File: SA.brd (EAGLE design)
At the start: 60 x 75 mm, 171 parts, among them CON1 RF_IN, CON2 PLL_OUT, CON3 SWD_CON, CON4 USB-C, IC1 RF_AMP, IC10 MCP6D11, IC11 MCP6D11, IC12 TAR5SB33, IC2 STW81200, IC3 ADL5380, IC4 TAR5SB33, IC5 STM32G431KB, IC6 SKY13453, IC7 NJG1809, IC8 SKY13453, IC9 NJG1809, J1 HW_PD, T1 X4B40L1, X1 25MHz, X2 25MHz, X3 12MHz

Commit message: ほぼ完成
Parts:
- removed R2: 10, my_rcl:1608
- added C82: 0.1u, my_rcl:1608C
- added C83: 100p, my_rcl:1608C
- added L10: 47nH, my_rcl:1005
- added R40: 10k, my_rcl:1608
- added SW1: BOOT0, my_rcl:SKRPACE010
- C25, C27, C55: value 22p -> 100p; device my_rcl:1608C -> my_rcl:1005
- C26, C28, C3, C31, C32, C54, C56, C57: device my_rcl:1608C -> my_rcl:1005
- C41: value 0.01u -> 1u
- C44: value 1u -> 10n
- DR1, DR2, DR3, DR4: value HOLE-3.2 -> HOLE-3.2-CON; device my_connector:HOLE_3.2 -> my_connector:HOLE_3.2_CON
- FIL1: value 5515LP15A730 -> 5515LP15A0730001E
- FIL6: value DEA162025LT-5046C1 -> DEA160960LT-5059A1
- FIL8: value DEA162300HT-8047A1 -> DEA162400HT-8053A1; device my_rcl:RF-FILTER-1608-TDK2 -> my_rcl:RF-FILTER-1608-TDK
- IC1: value RF_AMP -> ADL5611
- L1: value 150nH -> 47nH; device my_rcl:1608 -> my_rcl:1005
- L2, L3, L4, L5, L6, L7, L8, L9: value 10u -> 10uH
- R1: value DNP -> 50; device my_rcl:1608 -> my_rcl:1005
- R13, R14, R17, R18: device my_rcl:1608 -> my_rcl:1005
- moved CON3 3.00 mm to (56.0, 56.0)
- moved C31 2.50 mm to (16.5, 10.0)
- moved C32 2.50 mm to (16.5, 12.0)
- moved R13 2.50 mm to (13.0, 12.0)
- moved R14 2.50 mm to (13.0, 10.0)
- moved R1 2.46 mm to (7.00, 29.2)
- moved C62 2.02 mm to (17.5, 47.0), turned to 0 degrees
- moved C63 2.02 mm to (22.5, 47.0), turned to 180 degrees
- moved R10 2.02 mm to (22.5, 45.0), turned to 0 degrees
- moved R9 2.02 mm to (17.5, 45.0), turned to 180 degrees
- moved C60 2.00 mm to (28.5, 47.0), turned to 0 degrees
- moved C61 2.00 mm to (33.5, 47.0), turned to 180 degrees
- moved R7 2.00 mm to (28.5, 45.0), turned to 180 degrees
- moved R8 2.00 mm to (33.5, 45.0), turned to 0 degrees
- moved C3 1.03 mm to (7.00, 34.8)
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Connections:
- net N$23 renamed PLL_OUT
- removed net N$19: L1.1, R2.1
- new net N$23: L10.2, R1.2
- new net ST_BOOT0: IC5.31, R40.2, SW1.3, SW1.4
- new net ST_NRST: C82.1, IC5.4
- net +3V3: now also IC10.7, IC11.7
- net +3V3D: now also SW1.1, SW1.2
- net GND: now also C82.2, C83.2, FIL2.4, FIL3.1, FIL3.3, FIL4.4, FIL5.4, FIL6.4, FIL7.1, FIL7.3, FIL8.2, R40.1; no longer FIL3.2, FIL3.5, FIL7.4, FIL7.6, FIL8.1, FIL8.3, FIL8.6, IC10.7, IC11.7, IC5.31
- net MIX_IN: now also R8.1; no longer C61.1
- net MIX_IP: now also R7.1; no longer C60.1
- net MIX_QN: now also R10.1; no longer C63.1
- net MIX_QP: now also R9.1; no longer C62.1
- net N$32: now also C60.2; no longer R7.2
- net N$33: now also C61.2; no longer R8.2
- net N$47: now also FIL3.5; no longer FIL3.3
- net N$50: now also FIL7.6; no longer FIL7.3
- net N$51: now also FIL3.2, FIL8.1; no longer FIL3.1, FIL8.2
- net N$53: now also FIL8.3; no longer FIL8.5
- net N$55: now also FIL7.4; no longer FIL7.1
- net N$58: now also C60.1, R7.2; no longer C60.2, R7.1
- net N$59: now also C61.1, R8.2; no longer C61.2, R8.1
- net N$60: now also C62.1, R9.2; no longer C62.2, R9.1
- net N$61: now also C63.1, R10.2; no longer C63.2, R10.1
- net N$7: now also C62.2; no longer R9.2
- net N$9: now also C63.2; no longer R10.2
- net RF_IN: now also L10.1; no longer R1.2
- net VCC_HFAMP: now also C83.1, L1.1; no longer R2.2
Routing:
- net GND: track 61.4 -> 103.4 mm, vias 12 -> 368
- net ST_BOOT0: track 0.00 -> 14.2 mm
- net +3V3D: track 77.8 -> 88.3 mm, vias 4 -> 5
- net ST_NRST: track 0.00 -> 7.15 mm, vias 0 -> 2
- net +3V3: track 87.8 -> 93.4 mm
- net UART_TX: track 11.3 -> 8.32 mm
- net PLL_OUT1N: track 35.3 -> 32.6 mm
- net PLL_OUT1P: track 34.6 -> 31.9 mm
- net VCC_HFAMP: track 5.95 -> 8.55 mm
- net PLL_OUT: track 13.2 -> 15.3 mm
- net RFIN_SW1: track 69.0 -> 70.7 mm
- net N$23: track 0.00 -> 1.75 mm
- net FIL_SW4: track 61.9 -> 63.6 mm
- net FIL_SW3: track 65.1 -> 66.9 mm
- net N$19: track 1.70 -> 0.00 mm
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- added copper zone on layer 15, net GND
- added copper zone on layer 2, net GND

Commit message: OK
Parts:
- added D3: LED, my_rcl:D1608
- added R2: 1k, my_rcl:1608
- added TP1: +5V, my_connector:TESTPIN
- added TP2: GND, my_connector:TESTPIN
- IC5: value STM32G431KB -> STM32G431K
- moved C82 0.75 mm to (40.0, 63.0)
- moved C59 0.25 mm to (45.8, 44.2)
- moved C69 0.25 mm to (42.5, 48.2)
- moved C70 0.25 mm to (48.8, 48.0)
- moved IC12 0.25 mm to (45.8, 48.0)
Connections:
- new net N$19: IC5.13, R30.1
- new net N$73: IC5.9, R2.1
- net +5V: now also TP1.1
- net GND: now also D3.K, TP2.1
- net N$24: now also R31.1; no longer R30.1
- net N$25: now also R32.1; no longer R31.1
- net N$27: now also R33.1; no longer R32.1
- net N$28: now also D3.A, R2.2; no longer IC5.9, R33.1
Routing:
- net N$19: track 0.00 -> 37.8 mm
- net N$28: track 41.5 -> 4.75 mm
- net +5V: track 134.7 -> 142.1 mm
- net N$24: track 37.9 -> 41.4 mm, vias 0 -> 2
- net N$25: track 41.6 -> 39.3 mm, vias 2 -> 0
- net N$73: track 0.00 -> 1.89 mm
- net N$27: track 39.8 -> 40.9 mm
- net ST_NRST: track 7.15 -> 7.90 mm
- net GND: vias 368 -> 379

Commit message: STw81200
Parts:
- removed C28: 100p, my_rcl:1005
- removed L1: 47nH, my_rcl:1005
- removed L4: 10uH, my_rcl:2012
- removed X2: 25MHz, my_rcl:KC3225
- added ATT1: 3dB, my_ic:TFA16
- added C84: 10p, my_rcl:1608C
- added C85, C86, C88, C89: 0.1u, my_rcl:1608C
- added C87: 10u, my_rcl:2012
- added CON5: USB-C, my_connector:5077CR-16-SMC2-BK-TR
- added FIL9: DEA160787LT-5032A1, my_rcl:RF-FILTER-1608-TDK2
- added IC13: TLV3542, my_ic:SOP8-3
- added IC14, IC15: TAR5SB33, my_ic:SOT23-5
- added IC16: STM32G431K, my_ic:TQFP32-08
- added L11, L12: 10uH, my_rcl:2012-R
- added R41, R42, R44: 1k, my_rcl:1608
- added R43: 10k, my_rcl:1608
- added R45, R46, R47, R48: 39, my_rcl:1608
- added R49, R50: 5.1k, my_rcl:1608
- added TP3, TP5, TP6, TP7, TP8: GND, my_connector:TESTPIN
- added TP4: +5V, my_connector:TESTPIN
- C1: device my_rcl:1608C -> my_rcl:2012
- C13: value 47n -> 4.7n
- C14: value 10u -> 47n
- C15, C18: value 0.1u -> 100p; device my_rcl:1608C -> my_rcl:1005RF
- C16, C46, C51, C7, C82: value 0.1u -> 10u; device my_rcl:1608C -> my_rcl:2012
- C19, C20, C62, C63, C8: value 10u -> 0.1u
- C22: value 10p -> 100p; device my_rcl:1608C -> my_rcl:1005RF
- C23: value 10p -> 10u; device my_rcl:1608C -> my_rcl:2012
- C24: value DNP -> 10u; device my_rcl:1608C -> my_rcl:2012
- C25, C26, R1: device my_rcl:1005 -> my_rcl:1005RF
- C27: value 100p -> 10p; device my_rcl:1005 -> my_rcl:1608C
- C29: value 1000p -> DNP
- C3: value 22p -> 0.1u; device my_rcl:1005 -> my_rcl:1608C
- C30, C35, C36: value 1000p -> 100p; device my_rcl:1608C -> my_rcl:1005RF
- C31, C32: value 100p -> 10u; device my_rcl:1005 -> my_rcl:1608C
- C33: value 3300p -> 10u
- C34: value 470p -> 10u
- C37: value 1u -> 100p; device my_rcl:1608C -> my_rcl:1005RF
- C38: value 10u -> 100p; device my_rcl:2012 -> my_rcl:1005RF
- C39, C40: value 10u -> 1000p; device my_rcl:2012 -> my_rcl:1608C
- C41: value 1u -> 3300p
- C42: value 0.1u -> 3300p
- C43: value 0.1u -> 1000p
- C44: value 10n -> 1000p
- C45: value 10u -> 1n; device my_rcl:1608C -> my_rcl:1005
- C47, C75: value 0.1u -> 1u
- C48, C49: value 22p -> 1u
- C50: value 22p -> 10u; device my_rcl:1608C -> my_rcl:3216
- C52, C81: value 1u -> 0.1u
- C53: value 4.7n -> 10n
- C54, C55: value 100p -> 0.01u; device my_rcl:1005 -> my_rcl:1608C
- C56: value 100p -> 10u; device my_rcl:1005 -> my_rcl:2012
- C57: value 100p -> 0.1u; device my_rcl:1005 -> my_rcl:1608C
- C58: value 22p -> 0.1u
- C59: value 1u -> 100p; device my_rcl:1608C -> my_rcl:1005
- C60, C61: value 10u -> 0.01u
- C64: value 0.01u -> 1n; device my_rcl:1608C -> my_rcl:1005
- C65, C66, C67: value 0.01u -> 22p
- C68: value 0.1u -> 22p
- C69: value 10u -> 1n; device my_rcl:2012 -> my_rcl:1005
- C71: value 0.1u -> 1n; device my_rcl:1608C -> my_rcl:1005
- C77: value 10p -> 0.1u
- C78: value 10p -> 1u
- C79: device my_rcl:2012 -> my_rcl:1608C
- C80: value 10u -> 10p; device my_rcl:3216 -> my_rcl:1608C
- C83: value 100p -> 0.1u
- C9: value 0.1u -> 22p; device my_rcl:1608C -> my_rcl:1005RF
- CON1: value RF_IN -> DM_L
- CON2: value PLL_OUT -> RF_IN
- CON3: value SWD_CON -> PLL_OUT; device my_connector:SWD_CON -> my_connector:SMA-EDGE
- CON4: value USB-C -> SWD_CON; device my_connector:5077CR-16-SMC2-BK-TR -> my_connector:SWD_CON
- D1: value LOCK -> PWR
- D2: value PWR -> LED
- D3: value LED -> LOCK
- FB1, FB2, FB3, FB4, FB5: device my_rcl:1608-J -> my_rcl:1608-FB
- FB7: value FB -> (none)
- FIL5: value DEA162025LT-5046C1 -> DEA160960LT-5059A1
- FIL6: value DEA160960LT-5059A1 -> DEA165150HT-8025C2
- FIL7: value DEA160787LT-5032A1 -> DEA162400HT-8053A1; device my_rcl:RF-FILTER-1608-TDK2 -> my_rcl:RF-FILTER-1608-TDK
- FIL8: value DEA162400HT-8053A1 -> DEA162025LT-5046C1
- IC1: value ADL5611 -> QPC6044; device my_ic:SOT89 -> my_ic:QFN24-QPC6044
- IC10, IC11: value MCP6D11 -> SN74LVC1G66; device my_ic:MSOP8 -> my_ic:SOT23-5-2
- IC12: value TAR5SB33 -> TLV3542; device my_ic:SOT23-5 -> my_ic:SOP8-3
- IC2: value STW81200 -> SKY13453; device my_ic:VFQFPN36 -> my_ic:SKY13453
- IC3: value ADL5380 -> STW81200; device my_ic:LFCSP24 -> my_ic:VFQFPN36
- IC4: value TAR5SB33 -> ADL5611; device my_ic:SOT23-5 -> my_ic:SOT89
- IC5: value STM32G431K -> SKY13453; device my_ic:TQFP32-08 -> my_ic:SKY13453
- IC6: value SKY13453 -> QPC6044; device my_ic:SKY13453 -> my_ic:QFN24-QPC6044
- IC7: value NJG1809 -> ADL5380; device my_ic:EQFN18 -> my_ic:LFCSP24
- IC8: value SKY13453 -> MCP6D11; device my_ic:SKY13453 -> my_ic:MSOP8
- IC9: value NJG1809 -> MCP6D11; device my_ic:EQFN18 -> my_ic:MSOP8
- L10: value 47nH -> 10uH; device my_rcl:1005 -> my_rcl:2012-R
- L2: value 10uH -> 47nH; device my_rcl:2012 -> my_rcl:1005RF
- L3: value 10uH -> 47nH; device my_rcl:2012 -> my_rcl:1608-L
- L5, L6, L7, L8, L9: device my_rcl:2012 -> my_rcl:2012-R
- R10, R7, R8, R9: value 25 -> 360
- R11, R12: value DNP -> 25
- R13: value 50 -> 25; device my_rcl:1005 -> my_rcl:1608
- R14: value DNP -> 25; device my_rcl:1005 -> my_rcl:1608
- R15: value 120 -> 25; device my_rcl:1608 -> my_rcl:1005RF
- R16: value 120 -> 10k
- R17: value 25 -> 10k; device my_rcl:1005 -> my_rcl:1608-3
- R18: value 25 -> 10k; device my_rcl:1005 -> my_rcl:1608
- R19: value 1k -> 10k; device my_rcl:1608 -> my_rcl:1608-3
- R2: value 1k -> 50; device my_rcl:1608 -> my_rcl:1005RF
- R20: value 1k -> 25; device my_rcl:1608 -> my_rcl:1005RF
- R21, R22: value 10k -> DNP
- R23, R24: value 360 -> 120
- R25, R26: value 10k -> 1k
- R27: value 360 -> 47; device my_rcl:1608 -> my_rcl:1608-3
- R28, R29: value 10k -> 47; device my_rcl:1608 -> my_rcl:1608-3
- R30: value 39 -> 47; device my_rcl:1608-J -> my_rcl:1608-3
- R31, R32, R33: value 39 -> 1k; device my_rcl:1608-J -> my_rcl:1608-3
- R34: value 5.1k -> 1k; device my_rcl:1608 -> my_rcl:1608-3
- R35: value 5.1k -> 39
- R39: value 39 -> 1.5k
- R40: value 10k -> 1.5k
- R6: value 360 -> 50; device my_rcl:1608 -> my_rcl:1005RF
- X3: device my_rcl:KC3225 -> my_rcl:KC3225-CRYSTAL
- moved CON3 68.0 mm to (2.50, 14.0)
- moved C65 53.8 mm to (29.8, 71.5), flipped to the top, turned to 90 degrees
- moved C21 53.4 mm to (44.8, 18.5), flipped to the bottom
- moved R33 50.7 mm to (14.5, 68.0)
- moved R6 50.7 mm to (13.0, 10.0), turned to 0 degrees
- moved R30 47.4 mm to (23.5, 67.5), flipped to the bottom, turned to 180 degrees
- moved R31 47.3 mm to (26.5, 68.0)
- moved C22 46.5 mm to (10.8, 42.0)
- moved C78 46.5 mm to (6.25, 60.8), turned to 90 degrees
- moved R2 45.4 mm to (7.00, 29.8), turned to 90 degrees
- moved C42 45.4 mm to (20.0, 51.2), flipped to the top, turned to 0 degrees
- moved R34 43.9 mm to (24.5, 67.0), turned to 270 degrees
- moved R35 43.9 mm to (27.8, 71.5), turned to 90 degrees
- moved FB5 43.2 mm to (18.2, 40.0), flipped to the bottom
- moved FB7 43.2 mm to (55.0, 17.2), flipped to the top
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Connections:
- removed net N$55: FIL7.4, IC9.18
- new net DUMMY_LOAD: CON1.SIG, R1.2
- new net N$74: IC12.2, R27.2, R31.2
- new net N$75: IC12.5, IC8.4, R17.2
- new net N$76: IC12.1, R31.1, R35.1
- new net N$77: IC13.5, IC9.4, R19.2
- new net N$78: IC13.7, R34.1, R38.1
- new net N$79: IC12.7, R32.1, R36.1
- new net N$80: IC13.6, R30.2, R34.2
- new net N$81: IC13.1, R33.1, R37.1
- new net N$82: ATT1.SIG2, C25.2
- new net N$83: IC10.2, R25.1, R28.1
- new net N$84: IC10.1, R25.2, R27.1
- new net N$85: IC11.2, R26.1, R30.1
- new net N$86: IC11.1, R26.2, R29.1
- new net N$87: FIL3.5, IC1.8
- new net PGA_SW: IC10.4, IC11.4, IC16.9, R44.1
- net +3V3: now also C73.1, C77.1, C87.1, FB5.1, IC12.8, IC13.8, IC15.5, R39.2; no longer C38.1, C74.1, C75.1, FB7.1, IC10.3, IC10.7, IC11.3, IC11.7, IC4.5, R28.2
- net +3V3D: now also C82.1, C86.1, C88.1, C89.1, FB7.1, IC14.5, IC16.1, IC16.15, IC16.17; no longer C69.1, C71.1, C72.1, C73.1, FB5.1, IC12.5, IC5.1, IC5.15, IC5.17
- net +5V: now also C50.1, C56.1, C72.1, C75.1, C76.1, C78.1, D1.A, IC10.5, IC11.5, IC14.1, IC14.3, IC15.1, IC15.3, IC8.3, IC8.7, IC9.3, IC9.7, TP4.1; no longer C37.1, C59.1, C79.1, C80.1, D2.A, IC12.1, IC12.3, IC4.1, IC4.3
- net ADC_IN: now also C65.2, IC16.7, R35.2; no longer C49.2, IC5.7, R36.2
- net ADC_IP: now also C66.1, IC16.8, R36.2; no longer C48.1, IC5.8, R37.2
- net ADC_QN: now also C67.2, IC16.5, R37.2; no longer C50.2, IC5.5, R38.2
- net ADC_QP: now also C68.1, IC16.6, R38.2; no longer C58.1, IC5.6, R39.2
- net AMP_IN: now also C43.2, L10.2, R8.1; no longer C35.2, L7.2, R15.1
- net AMP_IP: now also C43.1, L9.2, R23.2, R7.1; no longer C35.1, L6.2, R15.2, R6.1
- net AMP_QN: now also C44.2, L12.2, R10.1, R24.1; no longer C36.2, L9.2, R16.1, R27.1
- net AMP_QP: now also C44.1, L11.2, R24.2, R9.1; no longer C36.1, L8.2, R16.2, R24.1
- net FILTER_IN: now also C30.2; no longer C57.2
- net FILTER_OUT: now also IC6.22; no longer IC9.3
- net FIL_SW1: now also IC1.17, IC16.28; no longer IC5.28, IC7.13
- net FIL_SW2: now also IC1.18, IC16.27; no longer IC5.27, IC7.12
- net FIL_SW3: now also IC16.19, IC6.17; no longer IC5.19, IC9.13
- net FIL_SW4: now also IC16.18, IC6.18; no longer IC5.18, IC9.12
- net GND: now also ATT1.GND, C13.2, C20.2, C21.1, C24.1, C27.2, C3.2, C49.2, C50.2, C54.2, C55.2, C56.2, C57.2, C60.2, C61.2, C62.2, C63.2, C65.1, C67.1, C7.2, C84.2, C85.2, C86.2, C87.2, C88.2, C89.2, CON3.G1, CON3.G2, CON3.G3, CON3.G4, CON4.3, CON5.A1,B12:GND, CON5.B1,A12:GND, CON5.SHILED1, CON5.SHILED2, CON5.SHILED3, CON5.SHILED4, CON5.SHILED5, CON5.SHILED6, CON5.SHILED7, CON5.SHILED8, D2.K, FIL7.4, FIL9.1, FIL9.2, FIL9.3, FIL9.5, IC1.1, IC1.10, IC1.12, IC1.13, IC1.15, IC1.19, IC1.20, IC1.21, IC1.23, IC1.24, IC1.3, IC1.4, IC1.6, IC1.7, IC1.9, IC1.HT, IC10.3, IC11.3, IC12.4, IC13.4, IC14.2, IC15.2, IC16.14, IC16.16, IC16.32, IC2.3, IC3.12, IC3.13, IC3.35, IC3.6, IC3.HT1, IC3.HT2, IC3.HT3, IC3.HT4, IC5.3, IC6.1, IC6.10, IC6.12, IC6.13, IC6.15, IC6.19, IC6.2, IC6.20, IC6.21, IC6.23, IC6.24, IC6.4, IC6.6, IC6.7, IC6.9, IC6.HT, IC7.11, IC7.18, IC7.20, IC7.23, IC7.8, IC8.6, IC9.6, R2.1, R22.1, R41.1, R42.1, R43.1, R49.1, R50.1, R6.1, TP3.1, TP5.1, TP6.1, TP7.1, TP8.1; no longer C14.2, C15.2, C18.1, C20.1, C21.2, C22.2, C37.2, C38.2, C39.2, C40.2, C41.2, C42.2, C43.2, C44.2, C49.1, C5.2, C50.1, C65.2, C67.2, C9.2, CON3.3, CON4.A1,B12:GND, CON4.B1,A12:GND, CON4.SHILED1, CON4.SHILED2, CON4.SHILED3, CON4.SHILED4, CON4.SHILED5, CON4.SHILED6, CON4.SHILED7, CON4.SHILED8, D3.K, FIL7.1, FIL7.3, FIL7.5, IC10.6, IC11.6, IC12.2, IC2.12, IC2.13, IC2.35, IC2.5, IC2.6, IC2.HT, IC3.1, IC3.11, IC3.14, IC3.17, IC3.18, IC3.2, IC3.20, IC3.23, IC3.7, IC3.8, IC5.14, IC5.16, IC5.32, IC7.10, IC7.15, IC7.4, IC7.9, IC8.3, IC9.1, IC9.10, IC9.14, IC9.15, IC9.17, IC9.2, IC9.4, IC9.5, IC9.7, IC9.9, IC9.HT, R12.1, R13.1, R14.1, R19.1, R20.1, R29.1, R34.1, R35.1, X2.2, X2.4
- net MIX_ADJ: now also IC7.19, R21.1, R22.2; no longer IC3.19, R11.1, R12.2
- net MIX_IN: now also IC7.4, R12.1; no longer IC3.4, R8.1
- net MIX_IP: now also IC7.3, R11.1; no longer IC3.3, R7.1
- net MIX_QN: now also IC7.15, R14.1; no longer IC3.15, R10.1
- net MIX_QP: now also IC7.16, R13.1; no longer IC3.16, R9.1
- net N$1: now also C15.1, IC2.4; no longer C54.1, IC8.4
- net N$10: now also C42.1, L11.1, L7.2; no longer C34.1, L4.2, L8.1
- net N$11: now also C42.2, L12.1, L8.2; no longer C34.2, L5.2, L9.1
- net N$12: now also IC3.10; no longer IC2.10
- net N$13: now also C5.1, IC3.1; no longer C6.1, IC2.1
- net N$14: now also C27.1, IC3.20; no longer C22.1, IC2.20, X2.1
- net N$15: now also C6.1, IC3.7; no longer C7.1, IC2.7
- net N$16: now also C29.1, IC3.21; no longer C23.1, C24.1, IC2.21, X2.3
- net N$17: now also C36.1, R15.1; no longer C26.1, R17.1
- net N$18: now also C38.1, R20.1; no longer C28.1, R18.1
- net N$19: now also IC16.10, R45.1; no longer IC5.13, R30.1
- net N$2: now also C14.2; no longer C13.2
- net N$20: now also C37.1, IC7.21; no longer C27.1, IC3.21
- net N$21: now also C29.2; no longer C24.2
- net N$22: now also C83.1, IC15.4; no longer C21.1, IC4.4
- net N$23: now also L2.2, R2.2; no longer L10.2, R1.2
- net N$24: now also IC16.11, R46.1; no longer IC5.12, R31.1
- net N$25: now also IC16.12, R47.1; no longer IC5.11, R32.1
- net N$26: now also C26.2, R6.2; no longer C32.2, R13.2
- net N$27: now also IC16.13, R48.1; no longer IC5.10, R33.1
- net N$28: now also D2.A, R44.2; no longer D3.A, R2.2
- net N$29: now also CON5.B5:CC2, R50.2; no longer CON4.B5:CC2, R34.2
- net N$3: now also C41.1, L5.2, L9.1; no longer C33.1, L2.2, L6.1
- net N$30: now also CON5.A5:CC1, R49.2; no longer CON4.A5:CC1, R35.2
- net N$31: now also IC3.4; no longer IC2.4
- net N$32: now also C31.2, C39.1, L5.1; no longer C29.1, C60.2, L2.1
- net N$33: now also C32.2, C39.2, L6.1; no longer C29.2, C61.2, L3.1
- net N$34: now also IC7.9, R15.2; no longer IC3.9, R17.2
- net N$35: now also IC7.10, R20.2; no longer IC3.10, R18.2
- net N$36: now also D1.K, R41.2; no longer D2.K, R20.2
- net N$37: now also D3.K, R42.2; no longer D1.K, R19.2
- net N$38: now also IC1.22; no longer IC7.3
- net N$39: now also C18.1, IC2.2; no longer C56.1, IC8.2
- net N$4: now also C37.2; no longer C27.2
- net N$40: now also C18.2, IC5.4; no longer C56.2, IC6.4
- net N$41: now also C30.1, IC5.6; no longer C57.1, IC6.6
- net N$42: now also C9.2, IC2.6; no longer C3.2, IC8.6
- net N$43: now also C15.2, IC4.1; no longer C54.2, IC1.1
- net N$44: now also C22.1, IC4.3, L3.2; no longer C55.1, IC1.3, L1.2
- net N$45: now also FIL5.1, IC1.5; no longer FIL2.1, IC7.16
- net N$46: now also IC1.14; no longer IC7.18
- net N$47: now also FIL2.1, IC1.11; no longer FIL3.5, IC7.8
- net N$48: now also FIL8.1; no longer FIL5.1
- net N$49: now also FIL6.3, IC6.8; no longer FIL6.1, IC7.6
- net N$50: now also FIL5.3, FIL9.6; no longer FIL6.3, FIL7.6
- net N$51: now also FIL7.1; no longer FIL8.1
- net N$52: now also FIL7.3, IC6.11; no longer FIL2.3, IC9.8
- net N$53: now also FIL9.4, IC6.14; no longer FIL8.3, IC9.16
- net N$54: now also FIL8.3, IC6.5; no longer FIL5.3, IC9.6
- net N$56: now also C35.2; no longer C25.2
- net N$57: now also C22.2, IC5.2; no longer C55.2, IC6.2
- net N$58: now also C31.1, R11.2; no longer C60.1, R7.2
- net N$59: now also C32.1, R12.2; no longer C61.1, R8.2
- net N$6: now also C41.2, L10.1, L6.2; no longer C33.2, L3.2, L7.1
- net N$60: now also C33.1, R13.2; no longer C62.1, R9.2
- net N$61: now also C34.1, R14.2; no longer C63.1, R10.2
- net N$62: now also IC8.8, R16.1, R7.2; no longer IC10.8, R21.1, R6.2
- net N$63: now also IC8.1, R17.1, R8.2; no longer IC10.1, R22.1, R23.2
- net N$64: now also IC12.3, IC8.5, R16.2; no longer IC10.5, R21.2, R36.1
- net N$65: now also IC13.2, R29.2, R33.2; no longer IC10.4, R22.2, R37.1
- net N$66: now also IC9.8, R18.1, R9.2; no longer IC11.8, R24.2, R25.1
- net N$67: now also IC9.1, R10.2, R19.1; no longer IC11.1, R26.1, R27.2
- net N$68: now also IC12.6, R28.2, R32.2; no longer IC11.4, R26.2, R39.1
- net N$69: now also IC13.3, IC9.5, R18.2; no longer IC11.5, R25.2, R38.1
- net N$7: now also C33.2, C40.1, L7.1; no longer C30.1, C62.2, L4.1
- net N$70: now also C81.1, IC14.4; no longer C70.1, IC12.4
- net N$71: now also C80.1, IC16.2; no longer C78.1, IC5.2
- net N$72: now also C84.1, IC16.3; no longer C77.1, IC5.3
- net N$73: now also FIL2.3, FIL6.1; no longer IC5.9, R2.1
- net N$8: now also C35.1, IC7.22; no longer C25.1, IC3.22
- net N$9: now also C34.2, C40.2, L8.1; no longer C30.2, C63.2, L5.1
- net PLL_ICP: now also C14.1, IC3.15; no longer C53.1, IC2.15
- net PLL_OUT: now also ATT1.SIG1, CON3.SIG; no longer C31.2, CON2.SIG, R14.2
- net PLL_OUT1N: now also C26.1, IC3.33; no longer C32.1, IC2.33
- net PLL_OUT1P: now also C25.1, IC3.34; no longer C31.1, IC2.34
- net PLL_OUT2N: now also C38.2, IC3.30; no longer C28.2, IC2.30
- net PLL_OUT2P: now also C36.2, IC3.31; no longer C26.2, IC2.31
- net PLL_SPI_CS: now also IC3.25, R48.2; no longer IC2.25, R33.2
- net PLL_SPI_MISO: now also D3.A, IC3.22, R46.2; no longer D1.A, IC2.22, R31.2
- net PLL_SPI_MOSI: now also IC3.23, R47.2; no longer IC2.23, R30.2
- net PLL_SPI_SCK: now also IC3.24, R45.2; no longer IC2.24, R32.2
- net PLL_VCTRL: now also IC3.11; no longer IC2.11
- net RFIN_SW1: now also IC16.29, IC2.5; no longer IC5.29, IC8.5
- net RFIN_SW2: now also IC16.30, IC5.5; no longer IC5.30, IC6.5
- net RF_IN: now also C9.1, CON2.SIG, L2.1; no longer C3.1, CON1.SIG, L10.1
- net ST_BOOT0: now also IC16.31, R43.2; no longer IC5.31, R40.2
- net ST_NRST: now also C85.1, IC16.4; no longer C82.1, IC5.4
- net SWCLK: now also CON4.1, IC16.24; no longer CON3.1, IC5.24
- net SWDIO: now also CON4.4, IC16.23; no longer CON3.4, IC5.23
- net UART_RX: now also CON4.2, IC16.25; no longer CON3.2, IC5.25
- net UART_TX: now also CON4.5, IC16.26; no longer CON3.5, IC5.26
- net USB_DM: now also CON5.A7:DN1, CON5.B7:DN2, IC16.21; no longer CON4.A7:DN1, CON4.B7:DN2, IC5.21
- net USB_DP: now also CON5.A6:DP1, CON5.B6:DP2, IC16.22; no longer CON4.A6:DP1, CON4.B6:DP2, IC5.22
- net USB_VBUS: now also CON5.A4,B9:VBUS, CON5.B4,A9:VBUS; no longer CON4.A4,B9:VBUS, CON4.B4,A9:VBUS
- net VCC_HFAMP: now also C47.1, C53.1, C59.1, L3.1; no longer C41.1, C44.1, C83.1, L1.1
- net VCC_MIX: now also C46.1, C52.1, C58.1, C63.1, C64.1, C69.1, C71.1, IC7.13, IC7.24, IC7.6, R21.2; no longer C40.1, C43.1, C47.1, C51.1, IC3.13, IC3.24, IC3.6, R11.2
- net VCC_OSC: now also C20.1, C79.1, FB7.2; no longer C17.1, C45.1, FB5.2
- net VCC_RFSW1: now also C49.1, C55.1, C61.1, FB5.2, IC2.1, IC5.1; no longer C66.1, C67.1, C81.1, FB7.2, IC6.1, IC8.1
- net VCC_RFSW2: now also C48.1, C54.1, C60.1, IC1.16, IC6.16; no longer C52.1, C64.1, C65.1, IC7.11, IC9.11
- net VCOM: now also C70.1, C74.1, IC8.2, IC9.2, R39.1, R40.2; no longer C68.1, C76.1, IC10.2, IC11.2, R28.1, R29.2
- net VIN_PLL: now also C45.1, C51.1, C57.1, C62.1, IC3.18, IC3.28, IC3.36, IC3.9; no longer C39.1, C42.1, C46.1, IC2.18, IC2.28, IC2.36, IC2.9
- net VREG_4V5: now also C3.1, C5.2, IC3.16, IC3.2, IC3.3, IC3.32; no longer C5.1, C6.2, IC2.16, IC2.2, IC2.3, IC2.32
- net VREG_DIG: now also C21.2, C24.2, IC3.26, IC3.27; no longer C18.2, C20.2, IC2.26, IC2.27
- net VREG_REF: now also C23.1, IC3.17, IC3.19; no longer C16.1, IC2.17, IC2.19
- net VREG_RF: now also C16.1, C17.1, IC3.29; no longer C14.1, C15.1, IC2.29
- net VREG_VCO: now also C6.2, C7.1, IC3.14, IC3.8; no longer C7.2, C9.1, IC2.14, IC2.8
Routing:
- net +5V: track 142.1 -> 180.9 mm, vias 5 -> 7
- net GND: track 103.4 -> 67.3 mm, vias 379 -> 525
- net PGA_SW: track 0.00 -> 28.8 mm, vias 0 -> 3
- net FIL_SW3: track 67.1 -> 78.7 mm
- net FIL_SW4: track 63.8 -> 75.1 mm
- net VCC_RFSW2: track 16.2 -> 25.3 mm
- net +3V3: track 93.4 -> 86.1 mm
- net VCC_MIX: track 38.2 -> 45.0 mm
- net N$49: track 8.57 -> 1.93 mm
- net N$79: track 0.00 -> 6.32 mm
- net N$55: track 6.30 -> 0.00 mm
- net N$16: track 11.4 -> 5.21 mm
- net N$77: track 0.00 -> 5.62 mm
- net N$78: track 0.00 -> 5.62 mm
- net N$80: track 0.00 -> 5.45 mm, vias 0 -> 1
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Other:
- board size 60 x 75 mm -> 60 x 80 mm
- board text added: "Spectrum Analyzer 7GHz"
- board text removed: "Spectrum Analyzer ver2"

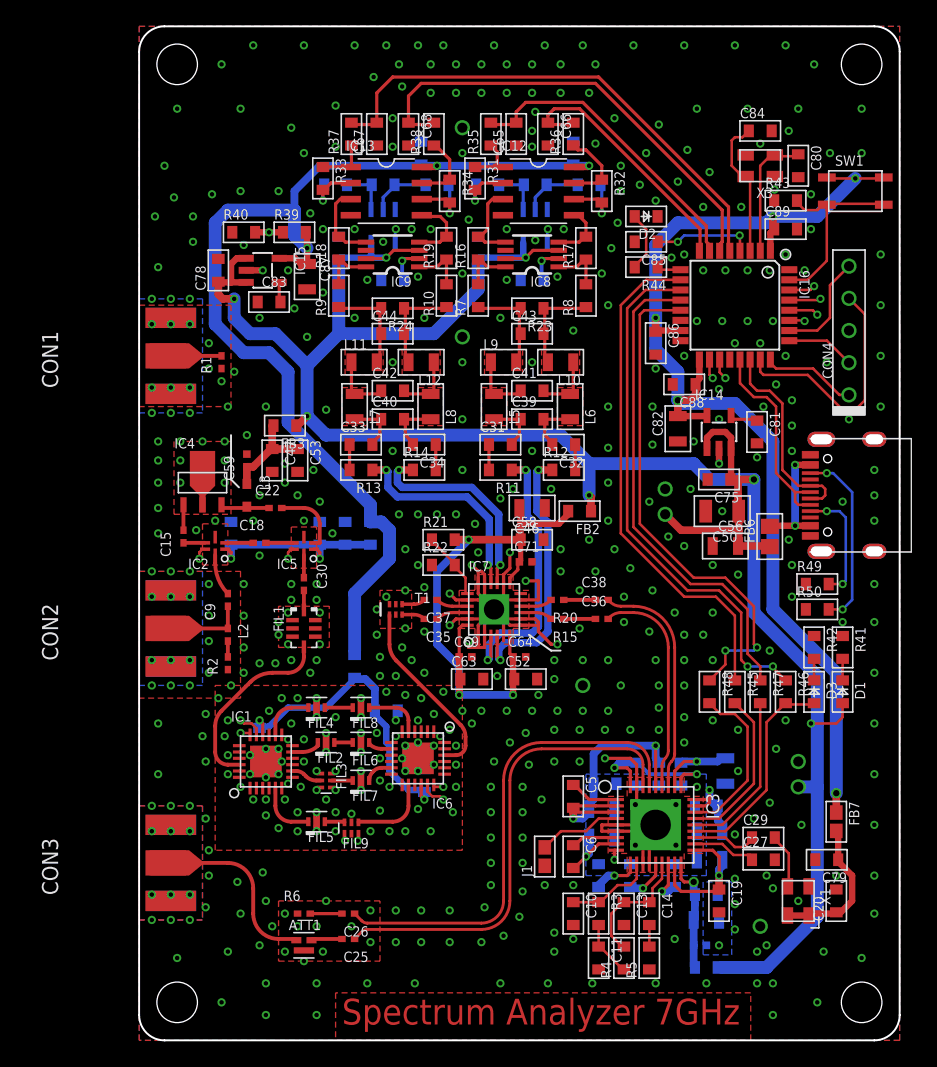
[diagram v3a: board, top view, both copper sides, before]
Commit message: PLLをLMX2572に
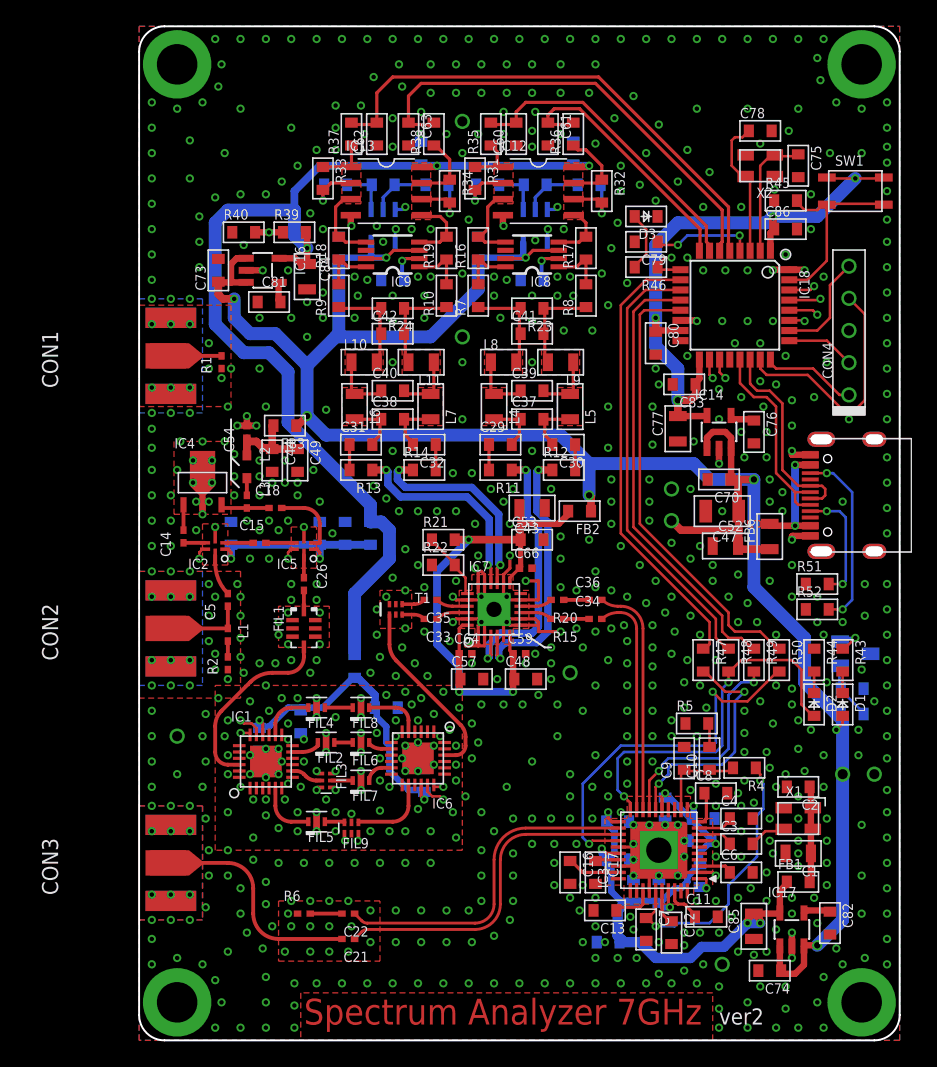
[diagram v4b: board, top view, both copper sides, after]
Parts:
- removed ATT1: 3dB, my_ic:TFA16
- removed C88, C89: 0.1u, my_rcl:1608C
- removed FB7: (no value), my_rcl:1608-J
- removed J1: HW_PD, my_rcl:1608-J
- removed L12: 10uH, my_rcl:2012-R
- added C28: 0.1u, my_rcl:1608C
- added IC17: TAR5SB33, my_ic:SOT23-5
- added IC18: STM32G431K, my_ic:TQFP32-08
- added L1: 47nH, my_rcl:1005RF
- added L4: 10uH, my_rcl:2012-R
- added R51, R52: 5.1k, my_rcl:1608
- added TP9: GND, my_connector:TESTPIN
- C10: value 680p -> 120n
- C11: value 4.7n -> 10n
- C13: value 4.7n -> 10u
- C14: value 47n -> 100p; device my_rcl:1608C -> my_rcl:1005RF
- C16: device my_rcl:2012 -> my_rcl:1608C
- C19, C70, C73, C74, C8: value 0.1u -> 1u
- C21: value 0.1u -> 100p; device my_rcl:1608C -> my_rcl:1005RF
- C23, C24, C82: value 10u -> 0.1u; device my_rcl:2012 -> my_rcl:1608C
- C25: value 100p -> 0.1u; device my_rcl:1005RF -> my_rcl:1608C
- C27, C80: value 10p -> 0.1u
- C29: value DNP -> 10u
- C3, C4: value 0.1u -> 1n
- C30: value 100p -> 10u; device my_rcl:1005RF -> my_rcl:1608C
- C33, C34: value 10u -> 100p; device my_rcl:1608C -> my_rcl:1005RF
- C37, C38: value 100p -> 1000p; device my_rcl:1005RF -> my_rcl:1608C
- C39, C40: value 1000p -> 3300p
- C41, C42: value 3300p -> 1000p
- C43: value 1000p -> 10u; device my_rcl:1608C -> my_rcl:2012
- C44: value 1000p -> 1u
- C45: value 1n -> 1u; device my_rcl:1005 -> my_rcl:1608C
- C46, C51, C87: value 10u -> 1u; device my_rcl:2012 -> my_rcl:1608C
- C47: value 1u -> 10u; device my_rcl:1608C -> my_rcl:3216
- C48: value 1u -> 0.1u
- C49: value 1u -> 10n
- C5: value 0.1u -> 22p; device my_rcl:1608C -> my_rcl:1005RF
- C50: value 10u -> 0.01u; device my_rcl:3216 -> my_rcl:1608C
- C52, C77, C85: value 0.1u -> 10u; device my_rcl:1608C -> my_rcl:2012
- C53: value 10n -> 0.1u
- C54: value 0.01u -> 100p; device my_rcl:1608C -> my_rcl:1005
- C56: value 10u -> 0.01u; device my_rcl:2012 -> my_rcl:1608C
- C58: value 0.1u -> 0.01u
- C59: value 100p -> 1n
- C6: value 0.1u -> 0.47u
- C60, C61: value 0.01u -> 22p
- C62, C63: value 0.1u -> 22p
- C65, C67, C68: value 22p -> 0.1u
- C66: value 22p -> 1n; device my_rcl:1608C -> my_rcl:1005
- C69, C71: value 1n -> 0.1u; device my_rcl:1005 -> my_rcl:1608C
- C7: value 10u -> 1.5n; device my_rcl:2012 -> my_rcl:1608C
- C75, C78: value 1u -> 10p
- C79: value 10u -> 0.1u
- C84: value 10p -> 10u; device my_rcl:1608C -> my_rcl:2012
- C9: value 22p -> 560p; device my_rcl:1005RF -> my_rcl:1608C
- D2: value LED -> LOCK
- D3: value LOCK -> LED
- DR1, DR2, DR3, DR4: value HOLE-3.2-CON -> HOLE-3.2C; device my_connector:HOLE_3.2_CON -> my_connector:HOLE_3.2_CON2
- FB6: device my_rcl:2012-J -> my_rcl:2012-R
- IC15: value TAR5SB33 -> TLV431; device my_ic:SOT23-5 -> my_ic:SC59
- IC16: value STM32G431K -> TAR5SB33; device my_ic:TQFP32-08 -> my_ic:SOT23-5
- IC3: value STW81200 -> LMX2572; device my_ic:VFQFPN36 -> my_ic:QFN40-LMX
- IC4: value ADL5611 -> SKY65017
- L2: value 47nH -> 100nH; device my_rcl:1005RF -> my_rcl:1608-L
- L3: value 47nH -> 33nH; device my_rcl:1608-L -> my_rcl:1005RF
- R3: value 220 -> 1k
- R39, R40: value 1.5k -> 5.1k
- R41: value 1k -> 10k
- R42: value 1k -> 3.6k
- R43: value 10k -> 1k
- R45: value 39 -> 10k
- R46: value 39 -> 1k
- R49, R50: value 5.1k -> 39
- R5: value 150 -> 330
- X1: value 25MHz -> 48MHz
- moved C74 57.6 mm to (49.8, 5.50), flipped to the top, turned to 180 degrees
- moved C87 57.6 mm to (37.0, 7.75), flipped to the bottom, turned to 0 degrees
- moved IC15 55.7 mm to (56.5, 30.5), flipped to the bottom, turned to 90 degrees
- moved C85 54.7 mm to (48.5, 9.00), turned to 270 degrees
- moved C62 54.5 mm to (18.8, 71.5), flipped to the top, turned to 90 degrees
- moved C60 51.9 mm to (29.8, 71.5), flipped to the top, turned to 90 degrees
- moved C79 50.8 mm to (40.0, 63.0)
- moved C14 47.3 mm to (3.50, 39.8), turned to 90 degrees
- moved C78 44.1 mm to (49.0, 71.8), turned to 0 degrees
- moved C63 43.3 mm to (21.2, 71.5), turned to 270 degrees
- moved C45 42.9 mm to (16.2, 40.0), turned to 90 degrees
- moved C82 40.8 mm to (54.5, 9.25)
- moved D2 40.7 mm to (53.2, 26.5), turned to 270 degrees
- moved C81 39.8 mm to (10.2, 58.2), turned to 180 degrees
- moved D3 39.8 mm to (40.0, 65.0), turned to 180 degrees
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- renumbered X3 to X2
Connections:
- removed net N$31: IC3.4, J1.2
- removed net N$82: ATT1.SIG2, C25.2
- removed net VIN_PLL: C45.1, C51.1, C57.1, C62.1, FB1.2, IC3.18, IC3.28, IC3.36, IC3.9
- removed net VREG_4V5: C1.1, C2.1, C3.1, C4.1, C5.2, IC3.16, IC3.2, IC3.3, IC3.32
- removed net VREG_DIG: C21.2, C24.2, IC3.26, IC3.27
- removed net VREG_REF: C19.1, C23.1, IC3.17, IC3.19
- removed net VREG_RF: C16.1, C17.1, IC3.29
- removed net VREG_VCO: C6.2, C7.1, C8.1, IC3.14, IC3.8
- new net N$55: C4.1, IC3.9
- new net N$88: C3.1, IC3.8
- new net N$89: C12.1, IC3.36
- new net N$90: C11.1, IC3.38
- new net N$91: C6.1, IC3.3
- new net N$92: C8.1, IC3.10
- new net N$93: C17.1, IC3.27
- new net PLL_EN: IC3.1, R3.1
- new net VCC_PLL: C19.1, C20.1, C23.1, C24.1, C25.1, C27.1, C28.1, C85.1, C87.1, FB1.1, IC17.5, IC3.11, IC3.15, IC3.21, IC3.26, IC3.37, IC3.7, R3.2
- net +3V3: now also C68.1, C72.1, C84.1, IC16.5; no longer C73.1, C77.1, C87.1, IC15.5
- net +3V3D: now also C77.1, C80.1, C83.1, IC18.1, IC18.15, IC18.17; no longer C82.1, C88.1, C89.1, FB7.1, IC16.1, IC16.15, IC16.17
- net +5V: now also C47.1, C52.1, C67.1, C70.1, C71.1, C73.1, C74.1, IC16.1, IC16.3, IC17.1, IC17.3, R41.2; no longer C50.1, C56.1, C72.1, C75.1, C76.1, C78.1, FB1.1, IC15.1, IC15.3
- net ADC_IN: now also C60.2, IC18.7; no longer C65.2, IC16.7
- net ADC_IP: now also C61.1, IC18.8; no longer C66.1, IC16.8
- net ADC_QN: now also C62.2, IC18.5; no longer C67.2, IC16.5
- net ADC_QP: now also C63.1, IC18.6; no longer C68.1, IC16.6
- net AMP_IN: now also C41.2, L9.2; no longer C43.2, L10.2
- net AMP_IP: now also C41.1, L8.2; no longer C43.1, L9.2
- net AMP_QN: now also C42.2, L11.2; no longer C44.2, L12.2
- net AMP_QP: now also C42.1, L10.2; no longer C44.1, L11.2
- net FILTER_IN: now also C26.2; no longer C30.2
- net FIL_SW1: now also IC18.28; no longer IC16.28
- net FIL_SW2: now also IC18.27; no longer IC16.27
- net FIL_SW3: now also IC18.19; no longer IC16.19
- net FIL_SW4: now also IC18.18; no longer IC16.18
- net GND: now also C24.2, C25.2, C28.2, C43.2, C44.2, C6.2, C60.1, C62.1, C65.2, C67.2, C9.2, D3.K, DR1.T, DR2.T, DR3.T, DR4.T, IC15.3, IC16.2, IC17.2, IC18.14, IC18.16, IC18.32, IC3.14, IC3.2, IC3.25, IC3.28, IC3.30, IC3.31, IC3.32, IC3.34, IC3.39, IC3.4, IC3.40, R44.1, R45.1, R51.1, R52.1, TP9.1; no longer ATT1.GND, C10.2, C21.1, C24.1, C3.2, C60.2, C62.2, C65.1, C67.1, C88.2, C89.2, D2.K, IC15.2, IC16.14, IC16.16, IC16.32, IC3.12, IC3.35, IC3.HT1, IC3.HT3, IC3.HT4, J1.1, R41.1, R43.1, R49.1, R50.1
- net N$1: now also C14.1; no longer C15.1
- net N$10: now also C40.1, L10.1, L6.2; no longer C42.1, L11.1, L7.2
- net N$11: now also C40.2, L11.1, L7.2; no longer C42.2, L12.1, L8.2
- net N$12: now also C16.1, IC3.29; no longer C12.1, IC3.10
- net N$13: now also C82.1, IC17.4; no longer C5.1, IC3.1
- net N$14: now also L2.2, L3.1; no longer C27.1, IC3.20
- net N$15: now also IC15.1, R41.1, R42.2; no longer C6.1, IC3.7
- net N$16: now also IC15.2, R43.1; no longer C29.1, IC3.21
- net N$17: now also C34.1; no longer C36.1
- net N$18: now also C36.1; no longer C38.1
- net N$19: now also IC18.10, R47.1; no longer IC16.10, R45.1
- net N$2: now also C10.2; no longer C14.2
- net N$20: now also C35.1; no longer C37.1
- net N$21: now also C3.2; no longer C29.2
- net N$22: now also C81.1, IC16.4; no longer C83.1, IC15.4
- net N$23: now also L1.2; no longer L2.2
- net N$24: now also IC18.11, R48.1; no longer IC16.11, R46.1
- net N$25: now also IC18.12, R49.1; no longer IC16.12, R47.1
- net N$26: now also C22.2; no longer C26.2
- net N$27: now also IC18.13, R50.1; no longer IC16.13, R48.1
- net N$28: now also D3.A, R46.2; no longer D2.A, R44.2
- net N$29: now also R52.2; no longer R50.2
- net N$3: now also C39.1, L4.2, L8.1; no longer C41.1, L5.2, L9.1
- net N$30: now also R51.2; no longer R49.2
- net N$32: now also C29.2, C37.1, L4.1; no longer C31.2, C39.1, L5.1
- net N$33: now also C30.2, C37.2, L5.1; no longer C32.2, C39.2, L6.1
- net N$36: now also R43.2; no longer R41.2
- net N$37: now also D2.K, R44.2; no longer D3.K, R42.2
- net N$39: now also C15.1; no longer C18.1
- net N$4: now also C35.2; no longer C37.2
- net N$40: now also C15.2; no longer C18.2
- net N$41: now also C26.1; no longer C30.1
- net N$42: now also C5.2; no longer C9.2
- net N$43: now also C14.2; no longer C15.2
- net N$44: now also C18.1; no longer C22.1
- net N$5: now also C13.1, IC3.33; no longer C11.1, R3.2, R4.1
- net N$56: now also C33.2; no longer C35.2
- net N$57: now also C18.2; no longer C22.2
- net N$58: now also C29.1; no longer C31.1
- net N$59: now also C30.1; no longer C32.1
- net N$6: now also C39.2, L5.2, L9.1; no longer C41.2, L10.1, L6.2
- net N$60: now also C31.1; no longer C33.1
- net N$61: now also C32.1; no longer C34.1
- net N$7: now also C31.2, C38.1, L6.1; no longer C33.2, C40.1, L7.1
- net N$70: now also C76.1; no longer C81.1
- net N$71: now also C75.1, IC18.2; no longer C80.1, IC16.2
- net N$72: now also C78.1, IC18.3; no longer C84.1, IC16.3
- net N$8: now also C33.1; no longer C35.1
- net N$9: now also C32.2, C38.2, L7.1; no longer C34.2, C40.2, L8.1
- net PGA_SW: now also IC18.9, R46.1; no longer IC16.9, R44.1
- net PLL_ICP: now also C10.1, C9.1, IC3.12; no longer C13.1, C14.1, IC3.15
- net PLL_OUT: now also C21.2; no longer ATT1.SIG1
- net PLL_OUT1N: now also C22.1, IC3.22; no longer C26.1, IC3.33
- net PLL_OUT1P: now also C21.1, IC3.23; no longer C25.1, IC3.34
- net PLL_OUT2N: now also C36.2, IC3.18; no longer C38.2, IC3.30
- net PLL_OUT2P: now also C34.2, IC3.19; no longer C36.2, IC3.31
- net PLL_SPI_CS: now also IC3.24, R50.2; no longer IC3.25, R48.2
- net PLL_SPI_MISO: now also D2.A, IC3.20, R48.2; no longer D3.A, IC3.22, R46.2
- net PLL_SPI_MOSI: now also IC3.17, R49.2; no longer IC3.23, R47.2
- net PLL_SPI_SCK: now also IC3.16, R47.2; no longer IC3.24, R45.2
- net PLL_VCTRL: now also C7.1, IC3.35, R4.1; no longer C10.1, IC3.11, R3.1
- net RFIN_SW1: now also IC18.29; no longer IC16.29
- net RFIN_SW2: now also IC18.30; no longer IC16.30
- net RF_IN: now also C5.1, L1.1; no longer C9.1, L2.1
- net ST_BOOT0: now also IC18.31, R45.2; no longer IC16.31, R43.2
- net ST_NRST: now also C79.1, IC18.4; no longer C85.1, IC16.4
- net SWCLK: now also IC18.24; no longer IC16.24
- net SWDIO: now also IC18.23; no longer IC16.23
- net UART_RX: now also IC18.25; no longer IC16.25
- net UART_TX: now also IC18.26; no longer IC16.26
- net USB_DM: now also IC18.21; no longer IC16.21
- net USB_DP: now also IC18.22; no longer IC16.22
- net VCC_HFAMP: now also C44.1, C49.1, C54.1, L2.1; no longer C47.1, C53.1, C59.1, L3.1
- net VCC_MIX: now also C43.1, C48.1, C53.1, C57.1, C59.1, C66.1; no longer C46.1, C52.1, C58.1, C63.1, C69.1, C71.1
- net VCC_OSC: now also C1.1, C2.1, FB1.2; no longer C20.1, C79.1, FB7.2
- net VCC_RFSW1: now also C45.1, C50.1, FB4.2; no longer C49.1, C61.1, FB5.2
- net VCC_RFSW2: now also C46.1, C51.1, C56.1, C58.1, FB5.2; no longer C48.1, C54.1, C60.1, FB4.2
- net VCOM: now also C65.1, C69.1; no longer C70.1, C74.1
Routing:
- net VCC_PLL: track 0.00 -> 58.6 mm, vias 0 -> 8
- net +3V3D: track 89.7 -> 49.5 mm, vias 5 -> 4
- net VREG_4V5: track 39.8 -> 0.00 mm, vias 3 -> 0
- net VIN_PLL: track 35.8 -> 0.00 mm, vias 4 -> 0
- net PLL_SPI_CS: track 13.2 -> 29.8 mm, vias 0 -> 2
- net PLL_VCTRL: track 6.92 -> 22.2 mm, vias 0 -> 2
- net VREG_VCO: track 15.1 -> 0.00 mm, vias 2 -> 0
- net PLL_SPI_MISO: track 16.8 -> 29.8 mm, vias 0 -> 2
- net VREG_REF: track 11.6 -> 0.00 mm, vias 1 -> 0
- net PLL_OUT1N: track 37.4 -> 26.2 mm
- net PLL_OUT1P: track 36.7 -> 26.2 mm
- net GND: track 67.3 -> 59.3 mm, vias 525 -> 824
- net VREG_DIG: track 7.16 -> 0.00 mm, vias 1 -> 0
- net N$24: track 42.0 -> 35.1 mm, vias 2 -> 0
- net VREG_RF: track 6.86 -> 0.00 mm, vias 1 -> 0
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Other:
- board text added: "ver2"

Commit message: 発注
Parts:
- C3, C4: device my_rcl:1608C -> my_rcl:1005
- IC4: device my_ic:SOT89 -> my_ic:SOT89-RF
- moved C3 0.90 mm to (48.0, 16.2)
- moved C4 0.50 mm to (48.0, 17.5)
- moved C2 0.12 mm to (52.0, 20.1)
- moved C75 0.12 mm to (52.1, 69.0)
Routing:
- net GND: track 59.3 -> 62.2 mm, vias 824 -> 936
- net VCC_RFSW2: track 25.1 -> 26.3 mm
- net N$55: track 2.80 -> 3.61 mm
- net +3V3: track 86.1 -> 85.3 mm
- net N$88: track 2.80 -> 3.30 mm
